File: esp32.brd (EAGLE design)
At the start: 160 x 100 mm, 2 parts, among them IC1 PEC11R-4230K-S0024, U1 ESP32-WROOM-32D

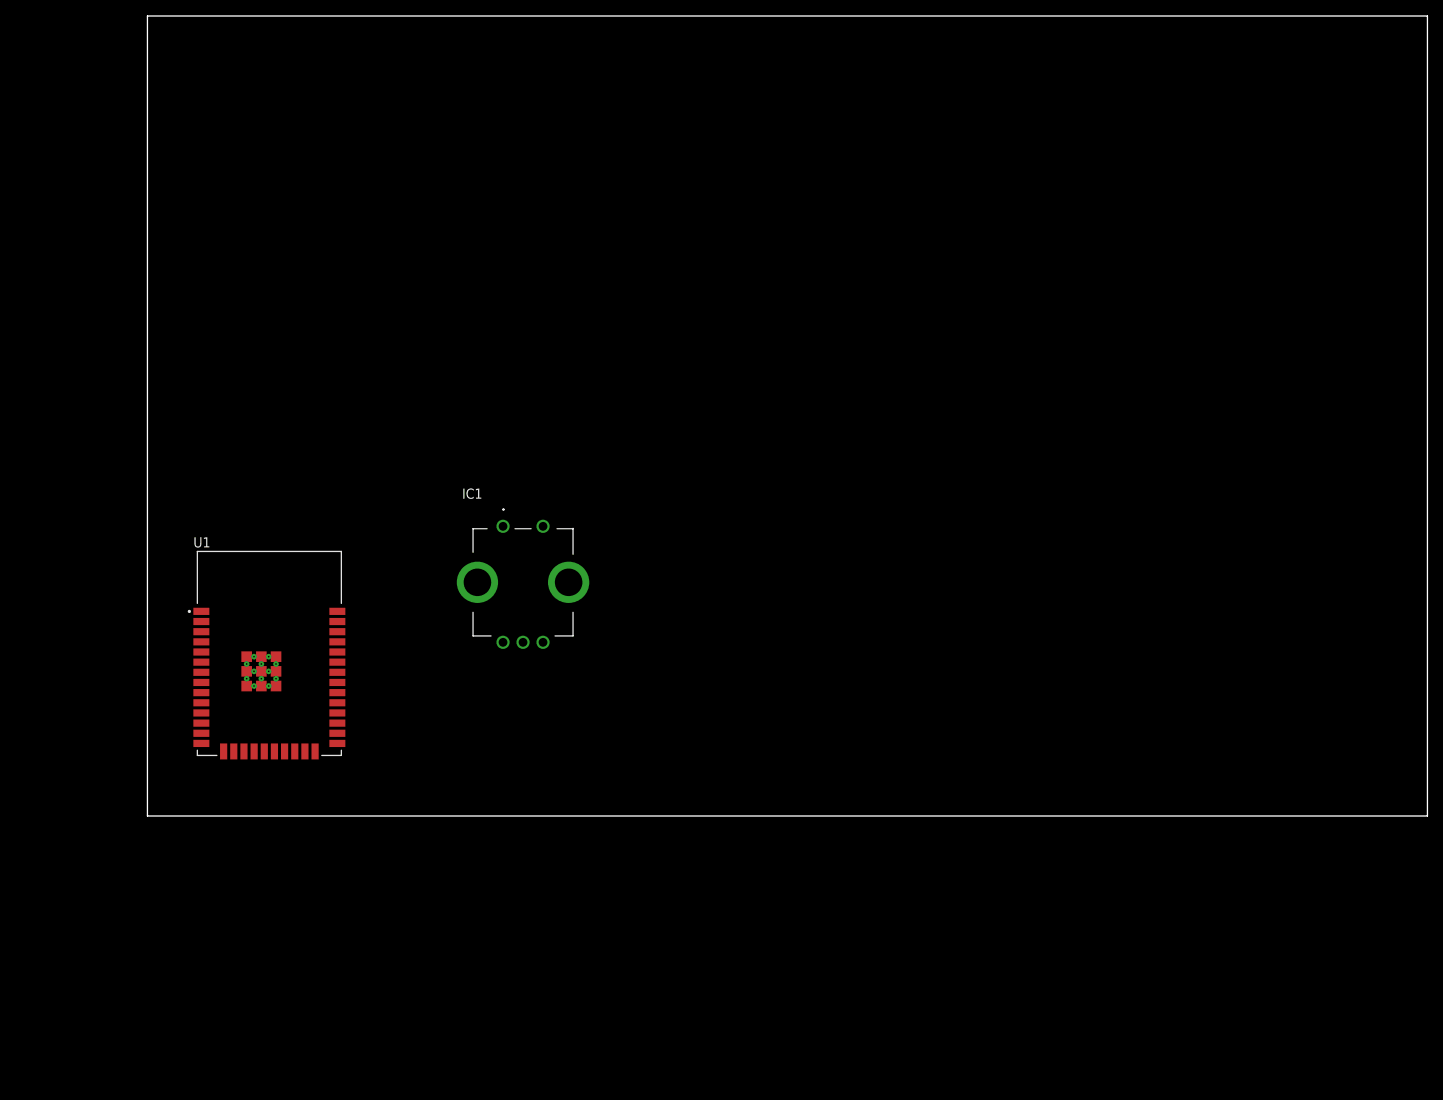
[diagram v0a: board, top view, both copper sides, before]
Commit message: Stora dela av schematic är klart. Saknar fortfarande vissa viktiga delar, men då måste jag passera admittansen först.
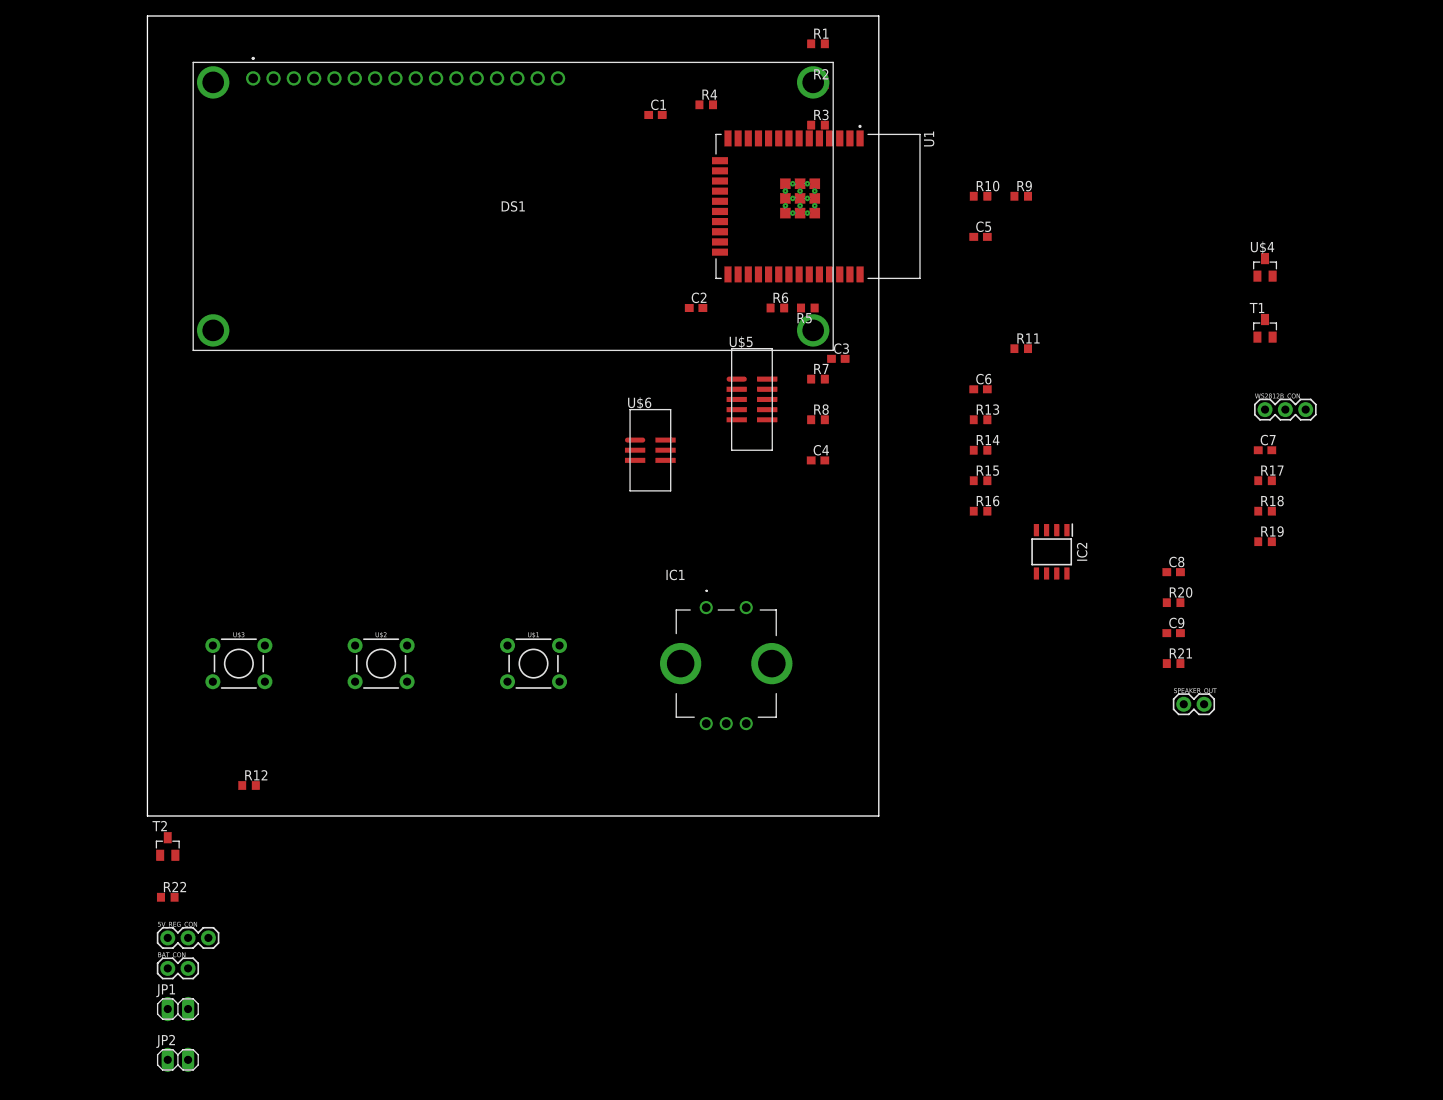
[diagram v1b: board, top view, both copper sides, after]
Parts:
- added 5V_REG_CON, WS2812B_CON: (no value), SparkFun-Connectors:1X03
- added BAT_CON, SPEAKER_OUT: (no value), SparkFun-Connectors:1X02
- added C1, C2, C3, C4, C5, C6: (no value), rcl:C0603
- added C7, C8: 10uF, rcl:C0603
- added C9: 270uF, rcl:C0603
- added DS1: (no value), Test:NHD0216XZFSWGBW_DUPONTCONNECTOR
- added IC2: AD8532ARZ, Test:SOIC127P600X175-8N
- added JP1, JP2: (no value), pinhead:1X02
- added R1, R10, R12, R14, R2, R3, R4, R5, R6, R8: 10k, rcl:R0603
- added R11, R13, R22, R7, R9: 100, rcl:R0603
- added R15, R16: (no value), rcl:R0603
- added R17, R18, R21: 50k, rcl:R0603
- added R19: 100k, rcl:R0603
- added R20: 16, rcl:R0603
- added T1, T2: BST82-1, Test:SOT23
- added U$1, U$2, U$3: PUSH_BUTTON, Test:TACTILE_SWITCH_PTH_6.0MM
- added U$4: A1SHB, Test:SOT23
- added U$5: ESP32_CON_JTAG, Test:DC3_10P_0.05
- added U$6: ESP32_CON_PROG, Test:DC3_6P_0.05
- moved U1 88.5 mm to (83.8, 76.2), turned to 270 degrees
- moved IC1 27.4 mm to (69.8, 19.1)
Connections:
- new net +3V3: IC1.1, R3.1, R4.1, U$1.1, U$1.2, U$2.1, U$2.2, U$3.1, U$3.2
- new net +5V: 5V_REG_CON.2, WS2812B_CON.1
- new net AUDIO_FROM_ESP32: C8.1
- new net BAT_MONITOR_ANALOG: R15.2, R16.1
- new net BAT_MONITOR_ENABLE: R13.2
- new net BTN_1: R7.1
- new net BTN_2: R9.1
- new net BTN_3: R11.1
- new net ENABLE_5V: R22.2
- new net ESP_EN: U$6.P$1
- new net ESP_IO_0: U$6.P$6
- new net ESP_RX: U$6.P$3
- new net ESP_TX: U$6.P$2
- new net N$1: IC1.A1, R1.2, R3.2
- new net N$10: C7.1, R17.1, R18.2
- new net N$11: R22.1, T2.1
- new net N$12: IC2.1, IC2.2, R20.2
- new net N$13: R13.1, T1.1
- new net N$14: C9.1, R20.1
- new net N$15: 5V_REG_CON.3, T2.3
- new net N$2: IC1.B1, R2.1, R4.2
- new net N$22: JP2.2, U$6.P$4
- new net N$23: JP2.1
- new net N$24: JP1.1, U$5.P$1
- new net N$25: JP1.2
- new net N$3: C4.1, R7.2, R8.2, U$1.3, U$1.4
- new net N$4: C8.2, IC2.3, R18.1, R19.2
- new net N$5: R15.1, U$4.3
- new net N$6: C5.1, R10.2, R9.2, U$2.3, U$2.4
- new net N$7: R14.2, T1.3, U$4.1
- new net N$8: C6.1, R11.2, R12.2, U$3.3, U$3.4
- new net N$9: C3.1, IC1.2, R5.2, R6.2
- new net ROT_ENC_A: C1.1, R1.1
- new net ROT_ENC_B: C2.1, R2.2
- new net ROT_ENC_BTN: R5.1
- new net SPEAKER_OUT: C9.2, R21.1, SPEAKER_OUT.1
- new net TCK: U$5.P$7
- new net TDI: U$5.P$9
- new net TDO: U$5.P$8
- new net TMS: U$5.P$6
- new net VCC: 5V_REG_CON.1, BAT_CON.1, IC2.8, R14.1, R17.2, U$4.2
- new net WS2812B_DATA: WS2812B_CON.2
- net GND: now also BAT_CON.2, C1.2, C2.2, C3.2, C4.2, C5.2, C6.2, IC1.C1, IC2.4, R10.1, R12.1, R16.2, R19.1, R21.2, R6.1, R8.1, SPEAKER_OUT.2, T1.2, T2.2, U$5.P$2, U$5.P$3, U$5.P$4, U$5.P$5, U$6.P$5, WS2812B_CON.3
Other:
- board size 160 x 100 mm -> 91.4 x 100 mm

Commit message: Lite grovt upplägg av vissa komponenter på kortet.
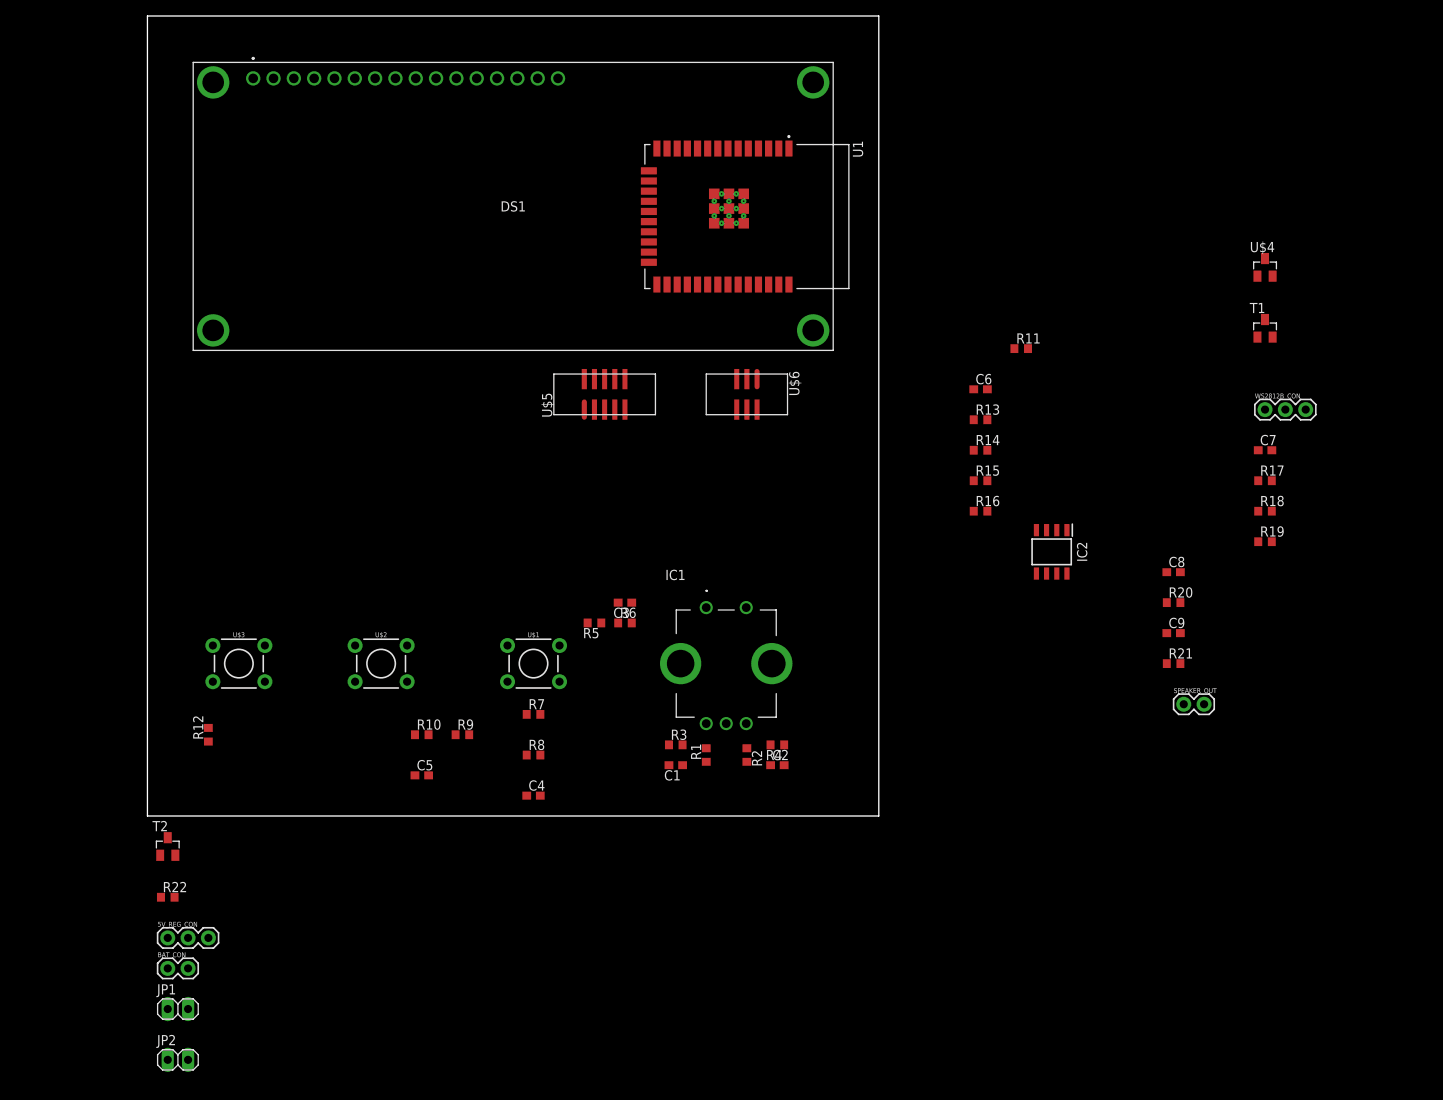
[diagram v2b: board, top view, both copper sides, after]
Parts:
- moved C5 97.0 mm to (34.3, 5.08)
- moved R10 97.0 mm to (34.3, 10.2)
- moved R9 97.0 mm to (39.4, 10.2)
- moved R1 90.0 mm to (69.8, 7.62), turned to 90 degrees
- moved R2 84.3 mm to (74.9, 7.62), turned to 270 degrees
- moved C1 81.3 mm to (66.0, 6.35), turned to 180 degrees
- moved R4 80.5 mm to (78.7, 8.89), turned to 180 degrees
- moved R3 79.5 mm to (66.0, 8.89)
- moved C2 58.0 mm to (78.7, 6.35)
- moved C4 55.0 mm to (48.3, 2.54)
- moved R7 55.0 mm to (48.3, 12.7)
- moved R8 55.0 mm to (48.3, 7.62)
- moved R5 47.6 mm to (55.9, 24.1)
- moved R6 43.7 mm to (59.7, 24.1)
- moved C3 40.5 mm to (59.7, 26.7), turned to 180 degrees
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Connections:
- removed net 3V3: U1.2
- net +3V3: now also U1.2
- net AUDIO_FROM_ESP32: now also U1.11
- net ESP_EN: now also U1.3
- net ESP_IO_0: now also U1.10
- net ESP_RX: now also U1.34
- net ESP_TX: now also U1.35
- net GND: now also C7.2
- net TCK: now also U1.16
- net TDI: now also U1.14
- net TDO: now also U1.23
- net TMS: now also U1.13

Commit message: Bra upplägg på kortet men saknar fortfarande 3.3V regulator.
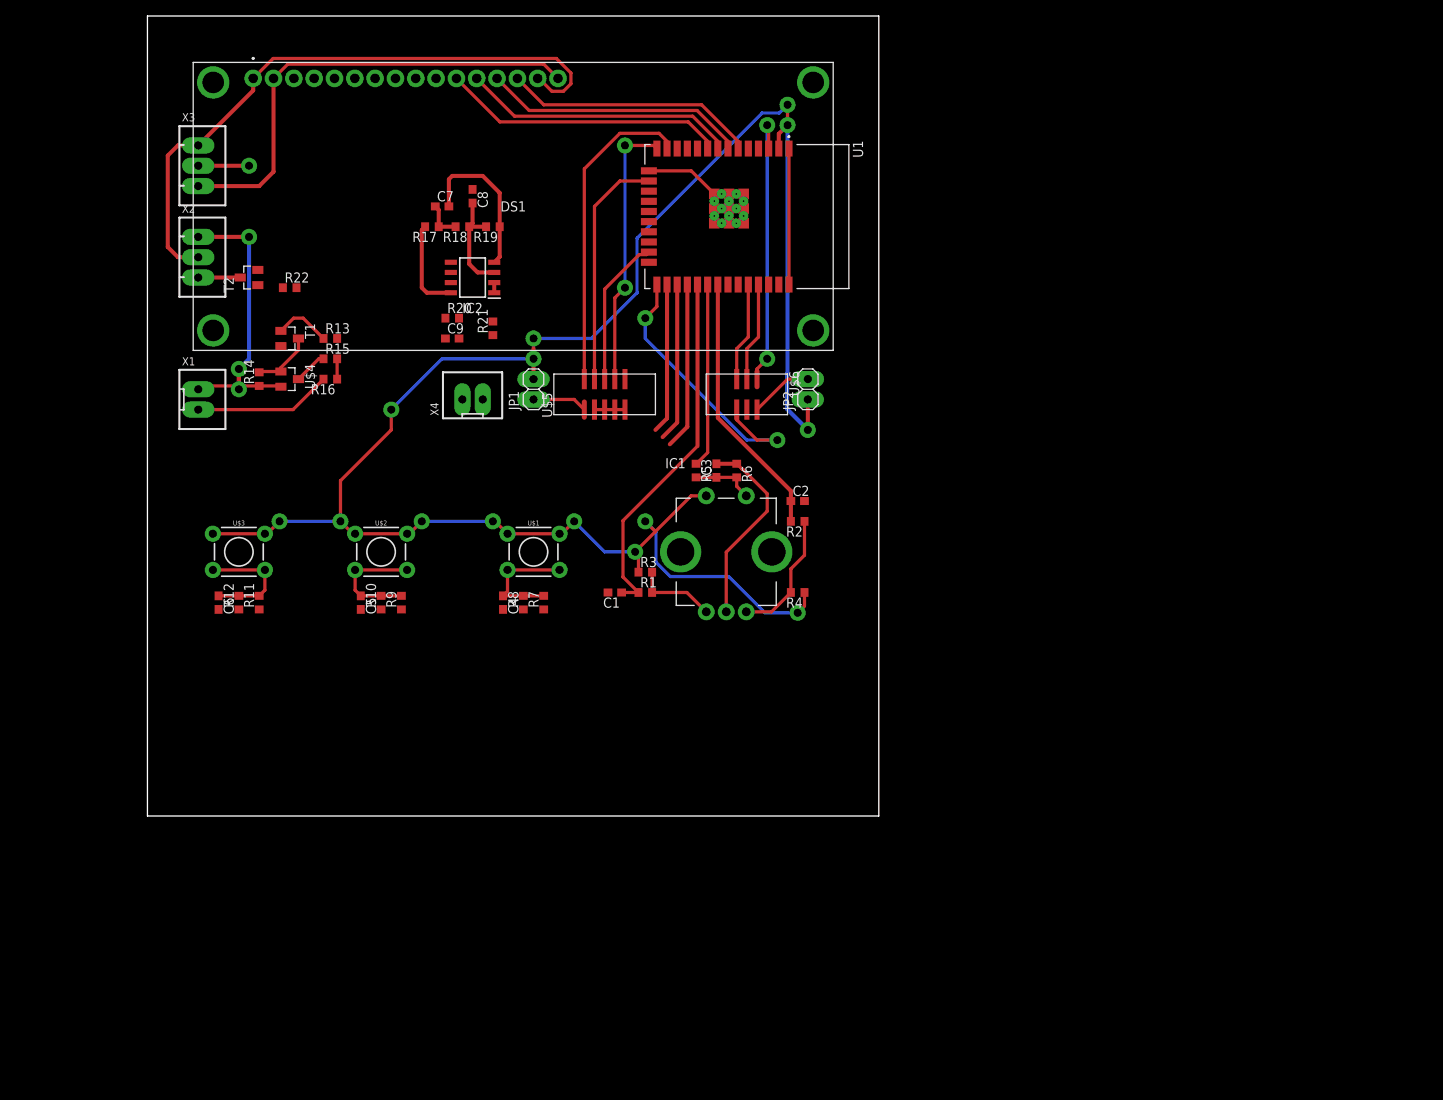
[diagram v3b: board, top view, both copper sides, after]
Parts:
- removed 5V_REG_CON, WS2812B_CON: (no value), SparkFun-Connectors:1X03
- removed BAT_CON, SPEAKER_OUT: (no value), SparkFun-Connectors:1X02
- added X1, X4: JST-XH-02-PIN-LONG-PAD, Rembrandt Electronics - JST XH Connectors v1-0:JST-XH-02-PACKAGE-LONG-PAD
- added X2, X3: JST-XH-03-PIN-LONG-PAD, Rembrandt Electronics - JST XH Connectors v1-0:JST-XH-03-PACKAGE-LONG-PAD
- moved U$4 122.7 mm to (17.8, 54.6), turned to 270 degrees
- moved T1 121.9 mm to (17.8, 59.7), turned to 270 degrees
- moved JP2 115.0 mm to (82.5, 53.3), turned to 90 degrees
- moved R17 108.9 mm to (35.6, 73.7), turned to 180 degrees
- moved C7 107.3 mm to (36.8, 76.2)
- moved R18 106.4 mm to (39.4, 73.7), turned to 180 degrees
- moved R19 104.2 mm to (43.2, 73.7), turned to 180 degrees
- moved R11 100.4 mm to (14.0, 26.7), turned to 90 degrees
- moved C8 99.4 mm to (40.6, 77.5), turned to 270 degrees
- moved C6 98.9 mm to (8.89, 26.7), turned to 270 degrees
- moved C9 97.4 mm to (38.1, 59.7)
- moved R20 96.9 mm to (38.1, 62.2)
- moved R21 94.9 mm to (43.2, 61.0), turned to 90 degrees
- moved R14 90.6 mm to (14.0, 54.6), turned to 90 degrees
- moved JP1 89.3 mm to (48.3, 53.3), turned to 90 degrees
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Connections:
- removed net N$23: JP2.1
- removed net N$25: JP1.2
- new net LCD_D4: DS1.11, U1.9
- new net LCD_D5: DS1.12, U1.8
- new net LCD_D6: DS1.13, U1.7
- new net LCD_D7: DS1.14, U1.6
- new net LCD_E: DS1.6
- new net LCD_RW: DS1.5
- new net N$20: DS1.4
- net +3V3: now also JP1.2, JP2.1
- net +5V: now also DS1.1, DS1.15, X2.2, X3.1; no longer 5V_REG_CON.2, WS2812B_CON.1
- net BTN_1: now also U1.28
- net BTN_2: now also U1.27
- net BTN_3: now also U1.26
- net ESP_IO_0: now also U1.25; no longer U1.10
- net GND: now also DS1.16, DS1.2, X1.2, X3.3, X4.2; no longer BAT_CON.2, SPEAKER_OUT.2, WS2812B_CON.3
- net N$15: now also X2.3; no longer 5V_REG_CON.3
- net ROT_ENC_A: now also U1.29
- net ROT_ENC_B: now also U1.31
- net ROT_ENC_BTN: now also U1.30
- net SPEAKER_OUT: now also X4.1; no longer SPEAKER_OUT.1
- net VCC: now also X1.1, X2.1; no longer 5V_REG_CON.1, BAT_CON.1
- net WS2812B_DATA: now also X3.2; no longer WS2812B_CON.2
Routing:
- net +3V3: track 0.00 -> 242.9 mm, vias 0 -> 14
- net GND: track 0.00 -> 150.8 mm
- net +5V: track 0.00 -> 79.4 mm
- net VCC: track 0.00 -> 50.3 mm, vias 0 -> 3
- net ROT_ENC_A: track 0.00 -> 45.3 mm
- net TMS: track 0.00 -> 39.8 mm
- net ESP_IO_0: track 0.00 -> 36.5 mm, vias 0 -> 2
- net LCD_D4: track 0.00 -> 35.6 mm
- net ESP_EN: track 0.00 -> 35.3 mm, vias 0 -> 2
- net LCD_D5: track 0.00 -> 34.3 mm
- net TDI: track 0.00 -> 33.9 mm, vias 0 -> 2
- net ROT_ENC_B: track 0.00 -> 33.4 mm
- net LCD_D6: track 0.00 -> 33.0 mm
- net LCD_D7: track 0.00 -> 31.8 mm
- net TCK: track 0.00 -> 29.7 mm
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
